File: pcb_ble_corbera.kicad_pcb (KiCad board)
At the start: 2 copper layers, 6 parts, among them J1 Conn_01x02, J2 Conn_01x02, U1 HDC1080, U11 BL652

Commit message: tweaks for pcb layout
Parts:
- removed U11: BL652, RF_Module:Laird_BL652
- added C1: 0.1uF, 16V, Capacitor_SMD:C_0805_2012Metric_Pad1.15x1.50mm_HandSolder, F.Cu at (198.1, 118.7)
- added C2: 100nF, Capacitor_SMD:C_0805_2012Metric_Pad1.15x1.50mm_HandSolder, F.Cu at (204.8, 107.4)
- added C3: 104pF, Capacitor_SMD:C_0805_2012Metric_Pad1.15x1.50mm_HandSolder, F.Cu at (199.7, 109.2)
- added D1: LED, LED_SMD:LED_0805_2012Metric, F.Cu at (195.2, 109.2)
- added J3: Conn_01x06, Connector_PinHeader_2.54mm:PinHeader_1x06_P2.54mm_Vertical, B.Cu at (149.9, 125.7)
- added J4: Conn_ARM_JTAG_SWD_10, Connector_PinHeader_1.27mm:PinHeader_2x05_P1.27mm_Vertical_SMD, F.Cu at (163.8, 118.1)
- added J6: Conn_01x18, Connector_PinHeader_2.54mm:PinHeader_1x18_P2.54mm_Vertical, B.Cu at (170.2, 82.5)
- added JP1: SolderJumper_2_Open, Jumper:SolderJumper-2_P1.3mm_Open_RoundedPad1.0x1.5mm, F.Cu at (197.5, 94.2)
- added R3: 220R, Resistor_SMD:R_0805_2012Metric_Pad1.15x1.50mm_HandSolder, F.Cu at (200.9, 100.0)
- added SW1: SW_DPST, Button_Switch_SMD:SW_MEC_5GSH9, F.Cu at (151.1, 109.2)
- added U2: HDC1080, Package_SON:Texas_PWSON-N6, F.Cu at (163.8, 104.1)
- J2: value Conn_01x02 -> Conn_01x18; footprint Connector_PinHeader_2.54mm:PinHeader_1x02_P2.54mm_Vertical -> Connector_PinHeader_2.54mm:PinHeader_1x18_P2.54mm_Vertical; moved to B.Cu
- U1: value HDC1080 -> BL652; footprint Package_SON:Texas_PWSON-N6 -> RF_Module:Laird_BL652
- moved R1 101.5 mm to (205.2, 101.7)
- moved R2 83.5 mm to (191.1, 109.2)
- moved J1 49.7 mm to (156.2, 108.0)
- moved U1 32.2 mm to (156.2, 88.9), turned to 270 degrees
- moved J2 30.1 mm to (143.5, 82.5), turned to 180 degrees
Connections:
- J2 pad 1: SDA -> VDD
- J2 pad 2: SCL -> SIO_25-SPI_CLK
- U1 pad 1: SDA -> GND
- U1 pad 2: GND -> SIO_24-SPI_MISO
- U1 pad 3: Net-(U1-Pad3) -> SIO_23-SPI_MOSI
- U1 pad 4: Net-(U1-Pad4) -> SIO_22
- U1 pad 5: VCC -> SWDIO-TMS
- U1 pad 6: SCL -> SWDCLK
- U1 pad 7: GND -> RESET

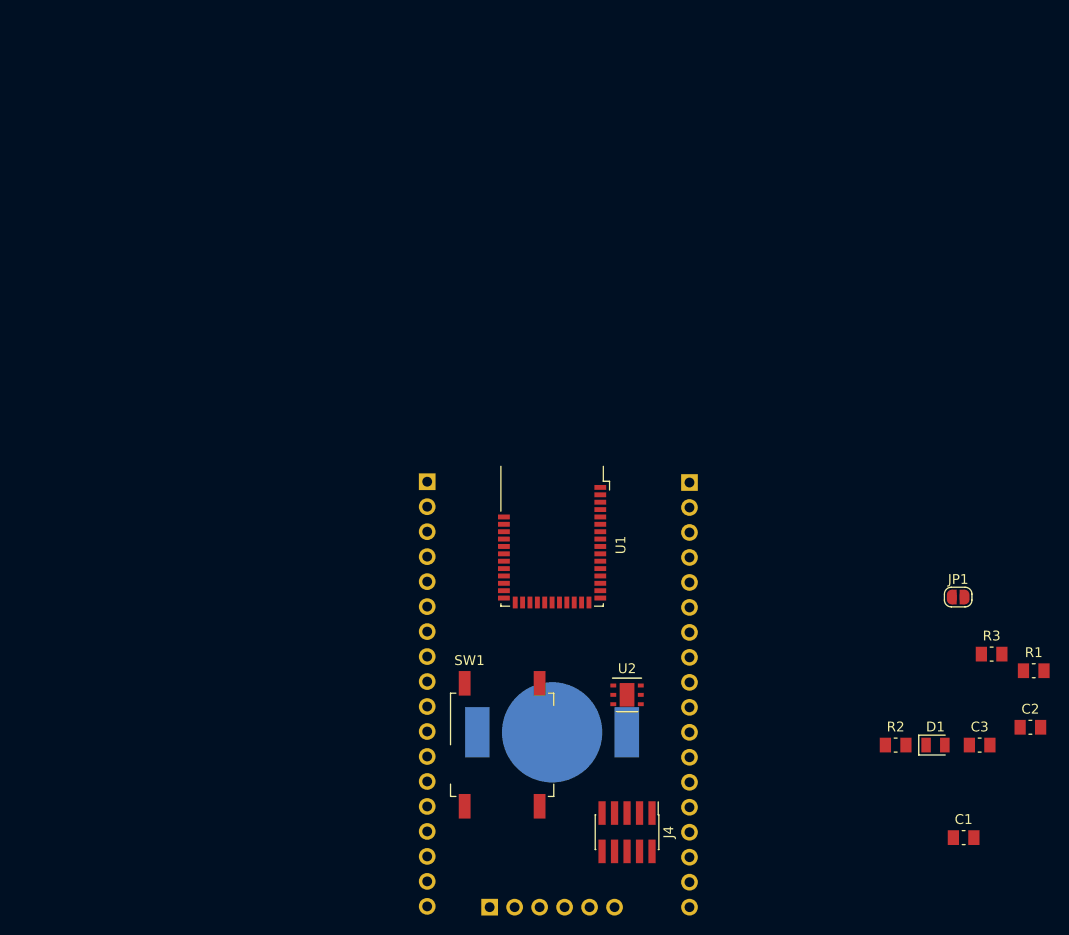
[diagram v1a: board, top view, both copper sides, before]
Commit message: reduced schematic, no header connectors
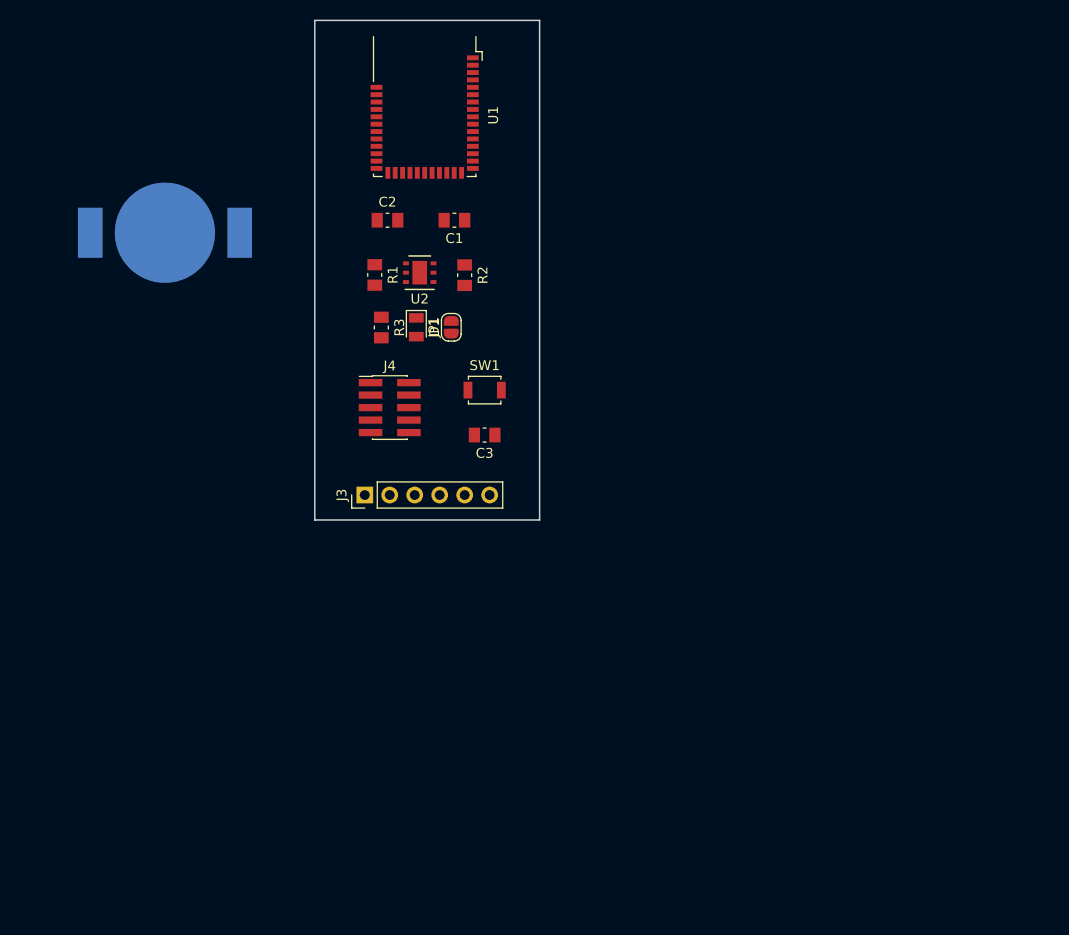
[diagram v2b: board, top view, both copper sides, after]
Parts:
- removed J2, J6: Conn_01x18, Connector_PinHeader_2.54mm:PinHeader_1x18_P2.54mm_Vertical
- J3: moved to F.Cu
- SW1: value SW_DPST -> SW_Push; footprint Button_Switch_SMD:SW_MEC_5GSH9 -> Button_Switch_SMD:SW_SPST_B3U-1000P
- moved C2 83.3 mm to (139.5, 55.9)
- moved C1 81.4 mm to (146.3, 55.9), turned to 180 degrees
- moved R1 78.2 mm to (138.2, 61.4), turned to 270 degrees
- moved R3 70.4 mm to (138.8, 66.8), turned to 270 degrees
- moved D1 67.8 mm to (142.4, 66.8), turned to 270 degrees
- moved R2 64.8 mm to (147.3, 61.5), turned to 270 degrees
- moved J1 64.3 mm to (116.8, 57.1)
- moved C3 59.4 mm to (149.4, 77.7), turned to 180 degrees
- moved JP1 58.4 mm to (146.0, 66.8), turned to 90 degrees
- moved J4 49.5 mm to (139.7, 74.9), turned to 0 degrees
- moved U2 47.8 mm to (142.7, 61.2), turned to 180 degrees
- moved U1 45.6 mm to (143.3, 45.2)
- moved J3 43.8 mm to (137.2, 83.8), turned to 90 degrees
- moved SW1 36.1 mm to (149.4, 73.2)
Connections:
- U1 pad 11: /BL652/SIO_16-SFLASH_MOSI -> SIO_14-SFLASH_MOSI
- U1 pad 22: SIO_03 -> BUTTON_0
- U1 pad 24: BUTTON_0 -> SIO_01
- U2 pad 7: GND -> (no net)
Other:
- board outline added: 22.9 x 50.8 mm
- net class Default: trace_width 0.25 -> 0.2
- net class Power added: clearance 0.15, trace_width 0.15, via_dia 0.6, via_drill 0.4
- rule trace_min: 0.2 -> 0.15
- rule via_min_size: 0.4 -> 0.15

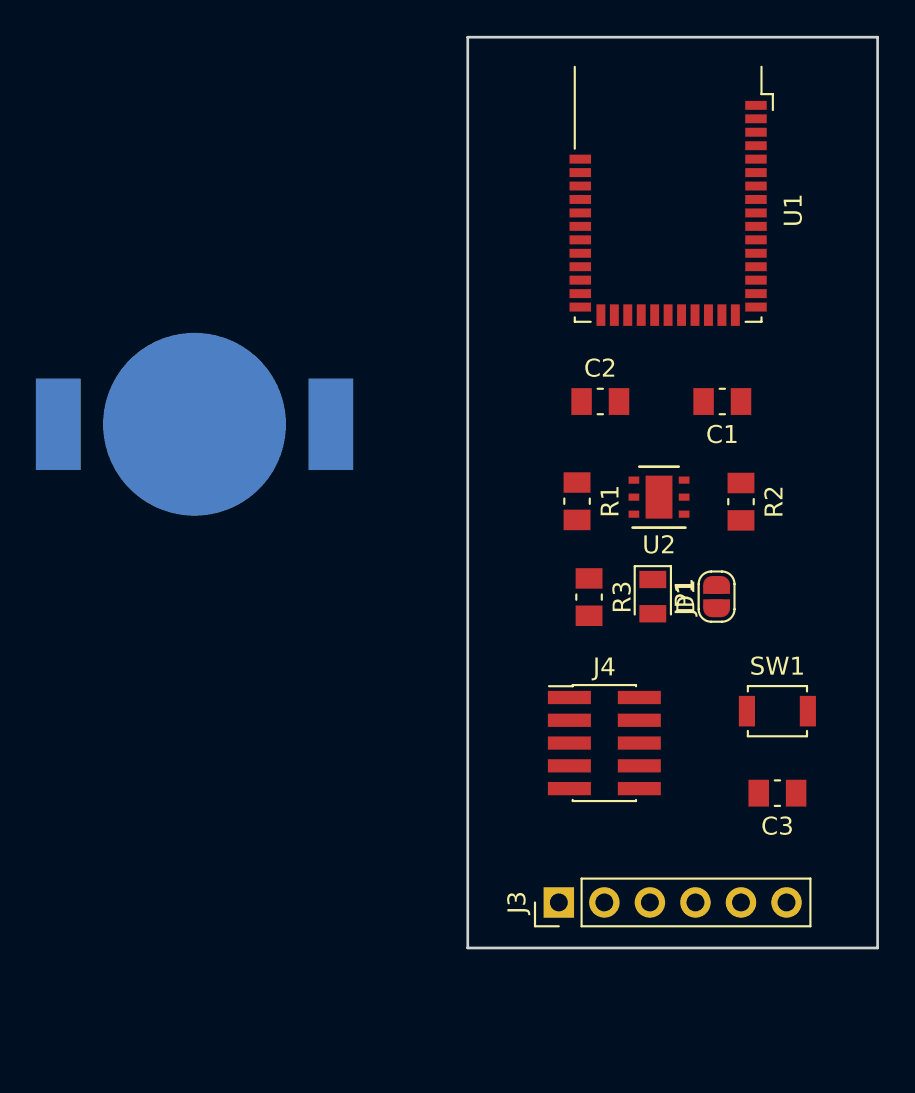
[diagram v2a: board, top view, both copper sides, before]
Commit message: changed battery, switch, debug conn
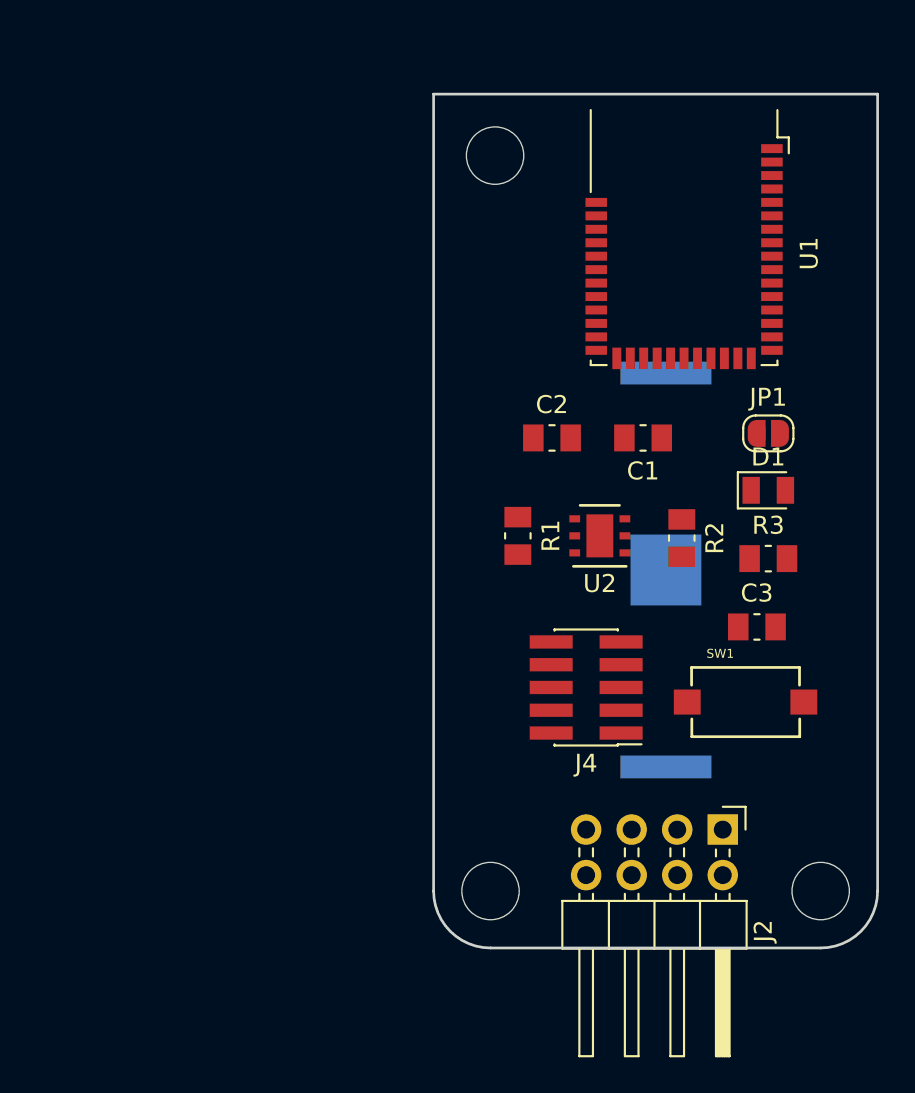
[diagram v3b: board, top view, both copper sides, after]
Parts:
- removed J3: Conn_01x06, Connector_PinHeader_2.54mm:PinHeader_1x06_P2.54mm_Vertical
- added J2: Conn_02x04_Odd_Even, Connector_PinHeader_2.54mm:PinHeader_2x04_P2.54mm_Horizontal, F.Cu at (146.3, 79.8)
- added REF**: MountingHole_3.2mm_M3_DIN965, MountingHole:MountingHole_3.2mm_M3_DIN965, B.Cu at (151.8, 83.2)
- added REF**: MountingHole_3.2mm_M3_DIN965, MountingHole:MountingHole_3.2mm_M3_DIN965, B.Cu at (133.3, 83.2)
- added REF**: MountingHole_3.2mm_M3_DIN965, MountingHole:MountingHole_3.2mm_M3_DIN965, B.Cu at (133.6, 42.2)
- J1: footprint Battery:BatteryHolder_LINX_BAT-HLD-012-SMT -> Battery_Holders:Keystone_3034_1x20mm-CoinCell
- SW1: footprint Button_Switch_SMD:SW_SPST_B3U-1000P -> _Project:SW_SMD_60X3.8
- moved J1 27.5 mm to (143.1, 65.3), turned to 90 degrees
- moved R3 10.2 mm to (148.8, 64.6), turned to 0 degrees
- moved JP1 9.55 mm to (148.8, 57.7), turned to 180 degrees
- moved C3 9.34 mm to (148.2, 68.5)
- moved D1 8.76 mm to (148.8, 60.8), turned to 0 degrees
- moved C1 4.86 mm to (141.9, 57.9)
- moved U2 3.95 mm to (139.4, 63.4)
- moved R2 3.88 mm to (144.0, 63.5)
- moved R1 3.83 mm to (134.9, 63.4)
- moved C2 3.37 mm to (136.8, 57.9)
- moved J4 3.26 mm to (138.7, 71.8), turned to 180 degrees
- moved U1 2.57 mm to (144.1, 47.6)
- moved SW1 1.85 mm to (147.6, 72.6)
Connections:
- U1 pad 17: SIO_08 -> SERIAL_RX
- U1 pad 19: SIO_06 -> SERIAL_RX
- U2 pad 7: (no net) -> GND
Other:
- board size 22.9 x 50.8 mm -> 24.8 x 47.6 mm

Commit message: new tracks
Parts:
- removed REF** (x3): MountingHole_3.2mm_M3_DIN965, MountingHole:MountingHole_3.2mm_M3_DIN965
- moved U1 47.9 mm to (138.8, 95.2), turned to 0 degrees
- moved C2 46.5 mm to (150.5, 102.3)
- moved R1 44.6 mm to (156.6, 102.3), turned to 0 degrees
- moved C1 41.5 mm to (150.5, 98.5), turned to 0 degrees
- moved J4 38.6 mm to (164.2, 100.8), turned to 270 degrees
- moved U2 38.4 mm to (156.6, 97.8), turned to 270 degrees
- moved J1 32.9 mm to (156.7, 95.2), turned to 180 degrees
- moved R2 32.3 mm to (156.6, 93.2), turned to 0 degrees
- moved D1 30.1 mm to (150.6, 90.9), turned to 180 degrees
- moved R3 30.1 mm to (150.5, 94.7)
- moved JP1 29.5 mm to (150.5, 87.1), turned to 0 degrees
- moved J2 27.3 mm to (170.8, 91.7), turned to 0 degrees
- moved SW1 24.2 mm to (165.2, 89.1), turned to 270 degrees
- moved C3 22.8 mm to (156.6, 89.6), turned to 0 degrees
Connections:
- J2 pad 4: SERIAL_RX -> SERIAL_TX
- U1 pad 17: SERIAL_RX -> SERIAL_TX
- U2 pad 7: GND -> Net-(U2-Pad7)
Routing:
- net GND: track 0.00 -> 92.1 mm, vias 0 -> 10
- net SWDIO-TMS: track 0.00 -> 57.5 mm, vias 0 -> 2
- net SWDCLK: track 0.00 -> 55.7 mm, vias 0 -> 2
- net VCC: track 0.00 -> 42.3 mm, vias 0 -> 4
- net SDA: track 0.00 -> 35.4 mm
- net SCL: track 0.00 -> 25.6 mm
- net BUTTON_0: track 0.00 -> 11.0 mm
- net (no net): vias 0 -> 4
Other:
- board size 24.8 x 47.6 mm -> 47.6 x 24.8 mm
- net class Default: trace_width 0.2 -> 0.1524; via_dia 0.8 -> 0.6
- net class Power: clearance 0.15 -> 0.25; trace_width 0.15 -> 0.254

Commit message: layout 90%
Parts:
- removed J1: Conn_01x02, Battery_Holders:Keystone_3034_1x20mm-CoinCell
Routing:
- net SERIAL_RX: track 0.00 -> 52.6 mm
- net SERIAL_TX: track 0.00 -> 45.1 mm, vias 0 -> 2
- net SIO_18: track 0.00 -> 38.5 mm, vias 0 -> 2
- net RESET: track 0.00 -> 32.9 mm, vias 0 -> 2
- net GND: track 92.1 -> 109.8 mm
- net BUTTON_0: track 11.0 -> 28.7 mm
- net VCC: track 42.3 -> 59.0 mm, vias 4 -> 9
- net LED_0: track 0.00 -> 9.63 mm, vias 0 -> 2
- net SWDIO-TMS: track 57.5 -> 66.3 mm
- net SWDCLK: track 55.7 -> 62.0 mm, vias 2 -> 6
- net Net-(D1-Pad1): track 0.00 -> 4.68 mm
- net SDA: track 35.4 -> 37.8 mm
- net SCL: track 25.6 -> 27.8 mm

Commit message: updates..
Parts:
- added J1: Conn_01x02, Battery_Holders:Keystone_3034_1x20mm-CoinCell, B.Cu at (151.6, 96.3)
- D1: footprint LED_SMD:LED_0805_2012Metric -> LED_SMD:LED_0805_2012Metric_Pad1.12x1.40mm_HandSolder
- JP1: footprint Jumper:SolderJumper-2_P1.3mm_Open_RoundedPad1.0x1.5mm -> TestPoint:SolderJumper-2_P1.3mm_Open_RoundedPad1.0x1.5mm
- moved SW1 2.06 mm to (163.5, 90.3)
- moved C1 1.35 mm to (149.2, 99.0)
- moved C2 1.35 mm to (149.2, 102.8)
- moved C3 1.35 mm to (155.3, 90.1)
- moved D1 1.35 mm to (149.3, 91.4)
- moved J2 1.35 mm to (169.6, 92.2)
- moved J4 1.35 mm to (163.0, 101.3)
- moved R1 1.35 mm to (155.3, 102.8)
- moved R2 1.35 mm to (155.4, 93.7)
- moved R3 1.35 mm to (149.2, 95.2)
- moved U1 1.35 mm to (137.6, 95.7)
- moved U2 1.35 mm to (155.3, 98.3)
- moved JP1 1.15 mm to (149.5, 87.7), turned to 180 degrees
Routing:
- net VCC: track 59.0 -> 70.5 mm, vias 9 -> 8
- net GND: track 109.8 -> 120.6 mm, vias 10 -> 12
- net SWDIO-TMS: track 66.3 -> 56.2 mm, vias 2 -> 4
- net Net-(D1-Pad2): track 0.00 -> 4.45 mm
- net LED_0: track 9.63 -> 12.8 mm
- net RESET: track 32.9 -> 35.1 mm, vias 2 -> 4
- net SWDCLK: track 62.0 -> 61.5 mm, vias 6 -> 5
- added copper zone on B.Cu, net GND
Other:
- board size 47.6 x 24.8 mm -> 48 x 25 mm

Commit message: added texts
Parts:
- added REF**: OSHW-Logo2_7.3x6mm_SilkScreen, Symbol:OSHW-Logo2_7.3x6mm_SilkScreen, B.Cu at (167.3, 87.0)
- added REF**: KiCad-Logo2_6mm_SilkScreen, Symbol:KiCad-Logo2_6mm_SilkScreen, B.Cu at (132.8, 95.5)
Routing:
- net GND: track 120.6 -> 125.8 mm, vias 12 -> 13
- net SERIAL_RX: track 52.7 -> 50.3 mm
- net VCC: track 70.5 -> 69.2 mm
- net SIO_18: track 39.0 -> 38.3 mm
- net SERIAL_TX: track 45.3 -> 44.7 mm
- added copper zone on F.Cu, net GND
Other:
- board text added: "@andreacalvo"
- board text added: "BLE Corbera v1.00 Temperature & Humidity Sensor"
- board text added: "https://github.com/andreacalvo/pcb_ble_corbera"
- board text added: "ραυηεт©2018"

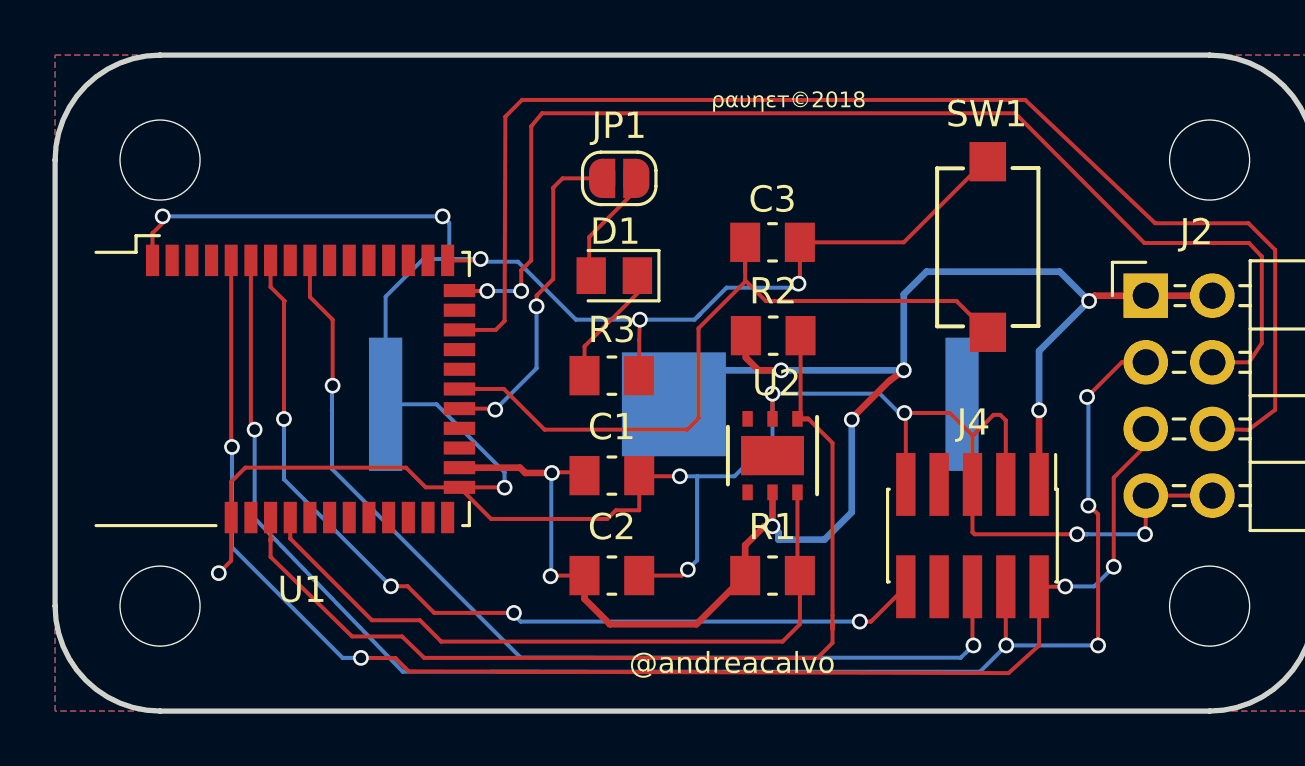
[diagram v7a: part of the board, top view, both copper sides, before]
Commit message: changed battery holder
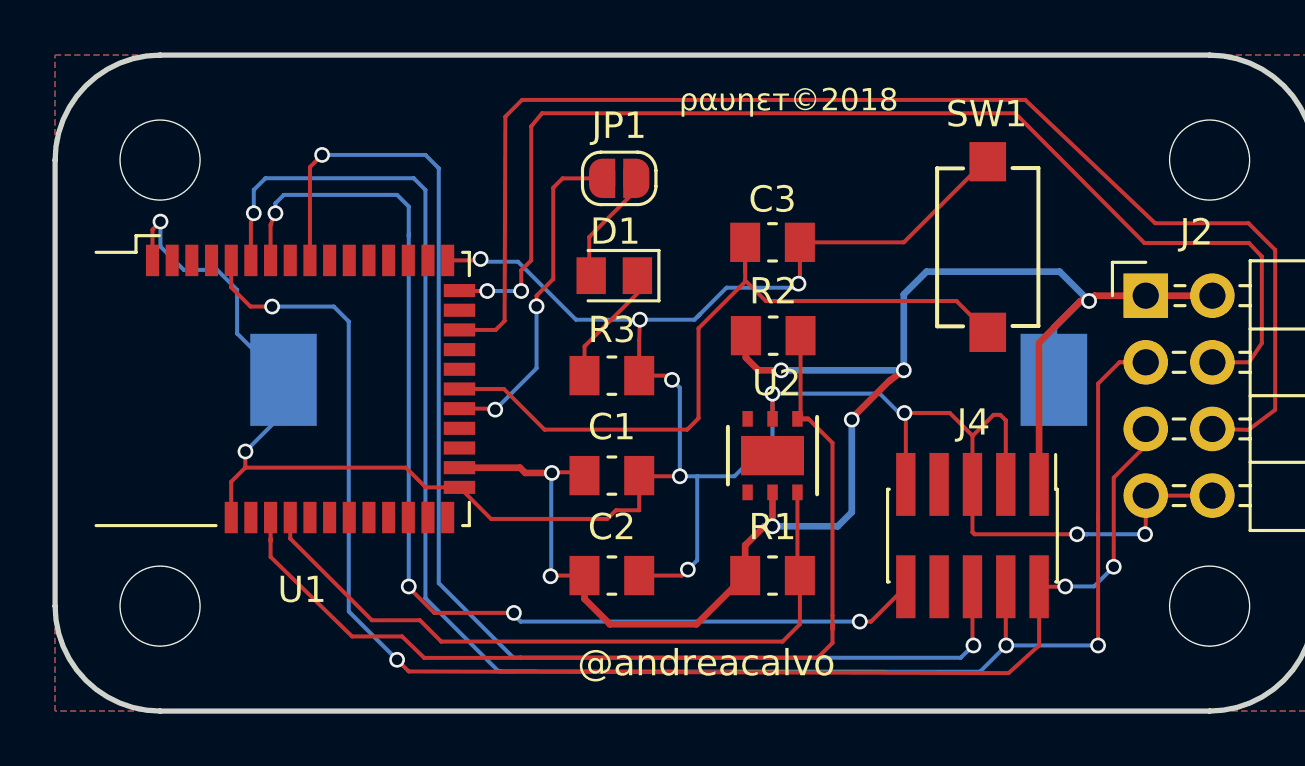
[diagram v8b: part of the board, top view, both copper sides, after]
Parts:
- removed the REF** at (167.3, 87.0)
- J1: footprint Battery_Holders:Keystone_3034_1x20mm-CoinCell -> Battery_Holders:Keystone_1058_1x2032-CoinCell
- moved REF** 1.08 mm to (131.8, 95.4)
- moved J1 0.95 mm to (151.4, 95.4)
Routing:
- net GND: track 125.8 -> 110.0 mm, vias 13 -> 12
- net SIO_18: track 38.3 -> 48.7 mm
- net RESET: track 35.1 -> 42.4 mm
- net SWDCLK: track 61.5 -> 68.7 mm, vias 5 -> 3
- net VCC: track 69.2 -> 66.5 mm, vias 8 -> 7
- net SWDIO-TMS: track 56.0 -> 56.7 mm
